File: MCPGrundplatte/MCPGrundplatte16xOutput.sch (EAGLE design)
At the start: 8 parts, among them IC1 ULN2803, IC4 ULN2803, X1GPA0-7 MKDSN1,5/9-5,08, X2 MKDSN1,5/2-5,08, X2GPB0-7 MKDSN1,5/9-5,08

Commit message: Aktuallisiert
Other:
- moved on the sheet: SV2, X1GPA0-7-1, X1GPA0-7-2, X1GPA0-7-3, X1GPA0-7-4, X1GPA0-7-5, X1GPA0-7-6, X1GPA0-7-7, X1GPA0-7-8, X1GPA0-7-9, X2-1, X2-2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

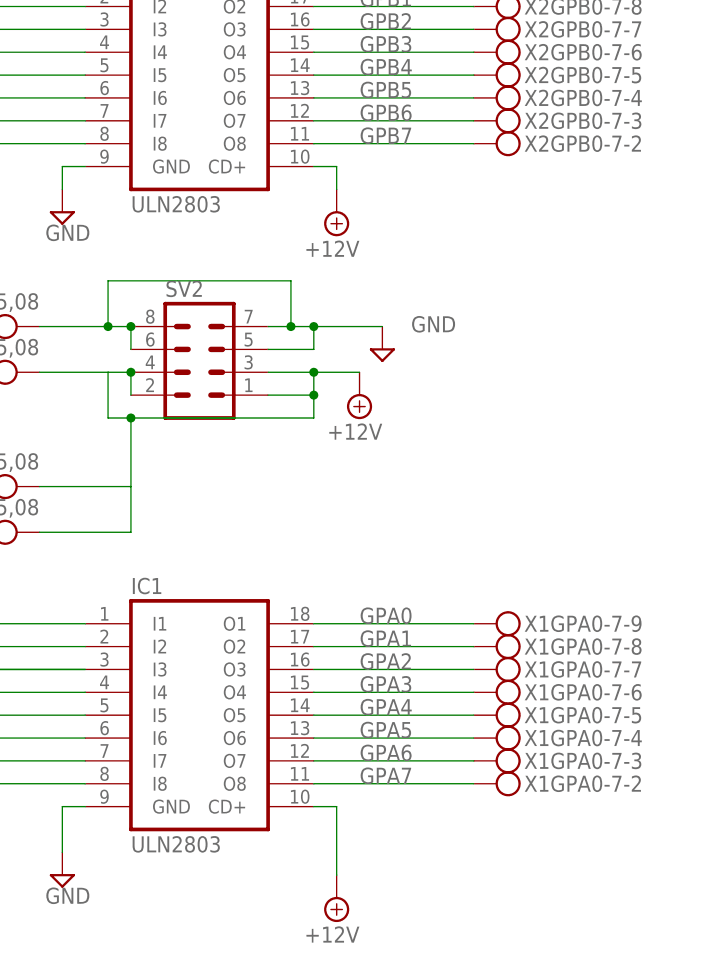
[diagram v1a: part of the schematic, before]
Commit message: Siebdruck angepasst, C hinzugefügt
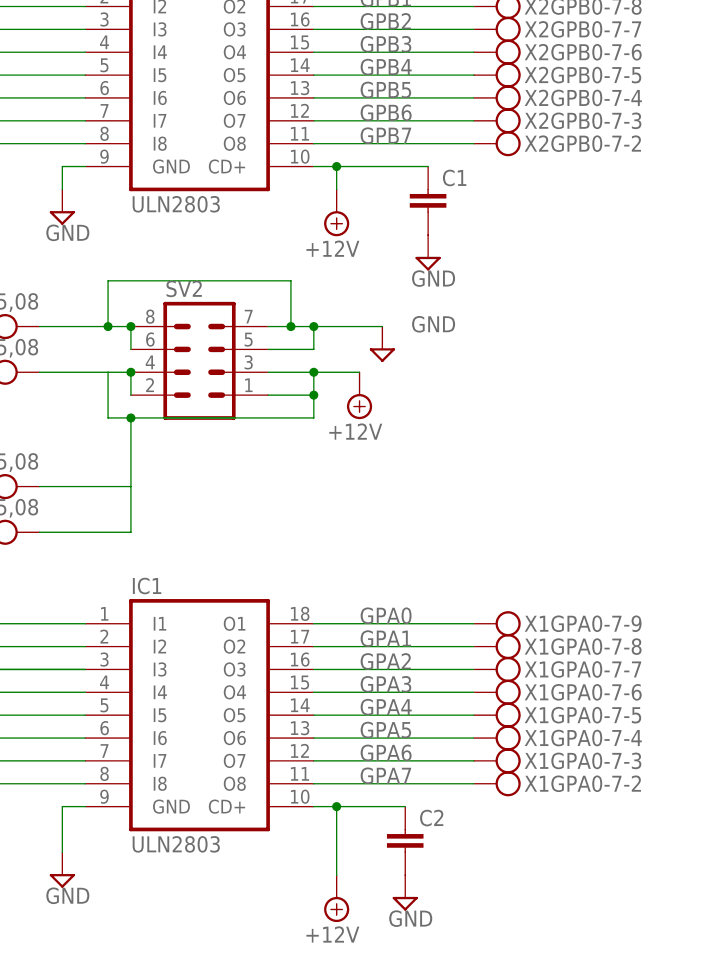
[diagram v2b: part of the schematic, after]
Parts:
- added C1, C2: (no value), rcl:C-EU025-024X044
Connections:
- net +12V: now also C1.1, C2.1
- net GND: now also C1.2, C2.2
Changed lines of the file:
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@@
 <part name="SUPPLY8" library="supply2" library_urn="urn:adsk.eagle:library:372" deviceset="+12V" device=""/>
 <part name="GND2" library="supply1" library_urn="urn:adsk.eagle:library:371" deviceset="GND" device=""/>
+<part name="C1" library="rcl" library_urn="urn:adsk.eagle:library:334" deviceset="C-EU" device="025-024X044" package3d_urn="urn:adsk.eagle:package:23630/1"/>
+<part name="C2" library="rcl" library_urn="urn:adsk.eagle:library:334" deviceset="C-EU" device="025-024X044" package3d_urn="urn:adsk.eagle:package:23630/1"/>
+<part name="SUPPLY4" library="supply2" library_urn="urn:adsk.eagle:library:372" deviceset="GND" device=""/>
+<part name="SUPPLY5" library="supply2" library_urn="urn:adsk.eagle:library:372" deviceset="GND" device=""/>
 </parts>
 <sheets>
@@
 <instance part="GND2" gate="1" x="48.26" y="-22.86" smashed="yes">
 <attribute name="VALUE" x="45.72" y="-27.94" size="1.778" layer="96"/>
+</instance>
+<instance part="C1" gate="G$1" x="127" y="27.94" smashed="yes">
+<attribute name="NAME" x="128.524" y="28.321" size="1.778" layer="95"/>
+<attribute name="VALUE" x="128.524" y="23.241" size="1.778" layer="96"/>
+</instance>
+<instance part="C2" gate="G$1" x="124.46" y="-43.18" smashed="yes">
+<attribute name="NAME" x="125.984" y="-42.799" size="1.778" layer="95"/>
+<attribute name="VALUE" x="125.984" y="-47.879" size="1.778" layer="96"/>
+</instance>
+<instance part="SUPPLY4" gate="GND" x="127" y="20.32" smashed="yes">
+<attribute name="VALUE" x="125.095" y="17.145" size="1.778" layer="96"/>
+</instance>
+<instance part="SUPPLY5" gate="GND" x="124.46" y="-50.8" smashed="yes">
+<attribute name="VALUE" x="122.555" y="-53.975" size="1.778" layer="96"/>
 </instance>
 </instances>
@@
 <pinref part="GND1" gate="1" pin="GND"/>
 </segment>
+<segment>
+<pinref part="C1" gate="G$1" pin="2"/>
+<pinref part="SUPPLY4" gate="GND" pin="GND"/>
+</segment>
+<segment>
+<pinref part="C2" gate="G$1" pin="2"/>
+<pinref part="SUPPLY5" gate="GND" pin="GND"/>
+</segment>
 </net>
 <net name="GPB0." class="0">
@@
 <wire x1="116.84" y1="-40.64" x2="116.84" y2="-48.26" width="0.1524" layer="91"/>
 <pinref part="SUPPLY6" gate="+12V" pin="+12V"/>
+<pinref part="C2" gate="G$1" pin="1"/>
+<wire x1="116.84" y1="-40.64" x2="124.46" y2="-40.64" width="0.1524" layer="91"/>
+<junction x="116.84" y="-40.64"/>
 </segment>
 <segment>
@@
 <wire x1="116.84" y1="30.48" x2="116.84" y2="27.94" width="0.1524" layer="91"/>
 <pinref part="SUPPLY8" gate="+12V" pin="+12V"/>
+<pinref part="C1" gate="G$1" pin="1"/>
+<wire x1="116.84" y1="30.48" x2="127" y2="30.48" width="0.1524" layer="91"/>
+<junction x="116.84" y="30.48"/>
 </segment>
 </net>
@@
 packages will not be understood (or retained) with this version.
 </note>
+<note version="8.4" severity="warning">
+Since Version 8.4, EAGLE supports properties for SPICE simulation.
+Probes in schematics and SPICE mapping objects found in parts and library devices
+will not be understood with this version. Update EAGLE to the latest version
+for full support of SPICE simulation.
+</note>
 </compatibility>
